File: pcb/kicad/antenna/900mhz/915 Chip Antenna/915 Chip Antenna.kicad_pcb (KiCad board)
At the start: 2 copper layers, 2 parts, among them P1 CONN_01X02, P2 CONN_01X02

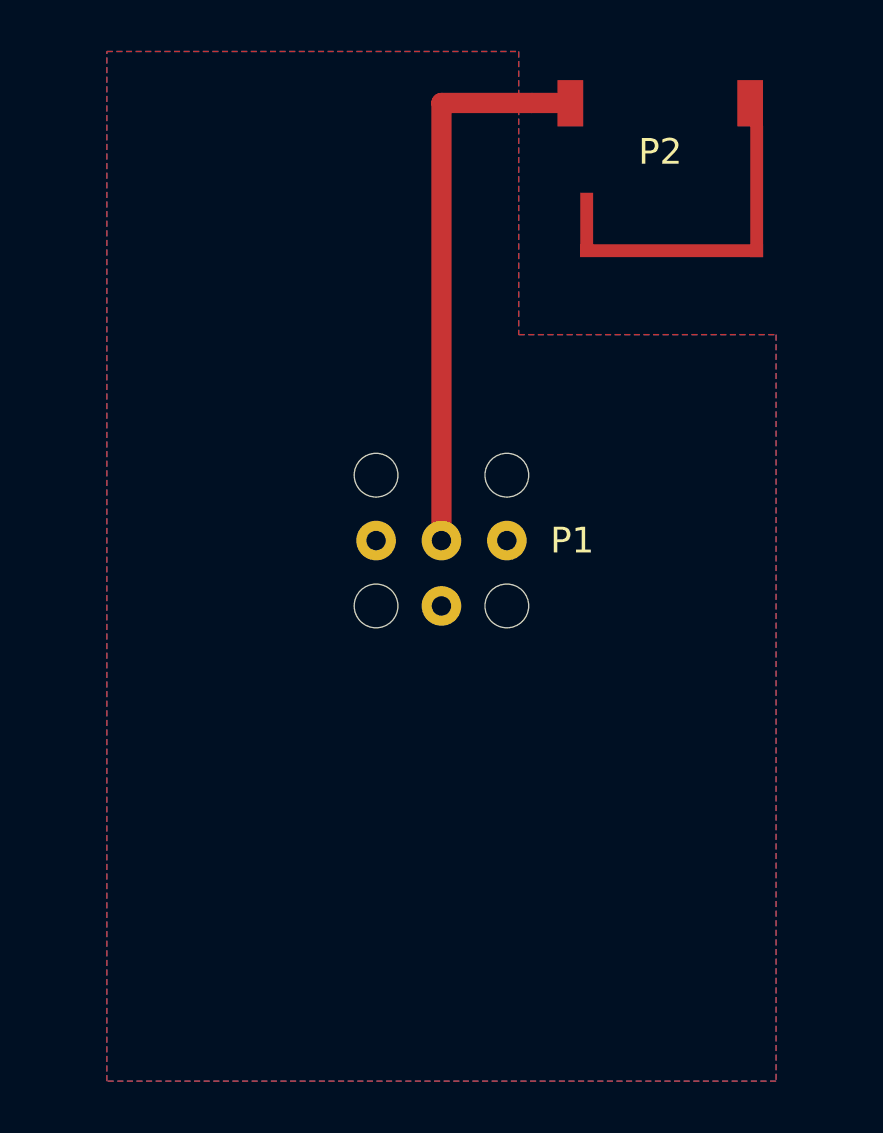
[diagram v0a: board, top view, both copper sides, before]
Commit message: Tile new antenna revisions
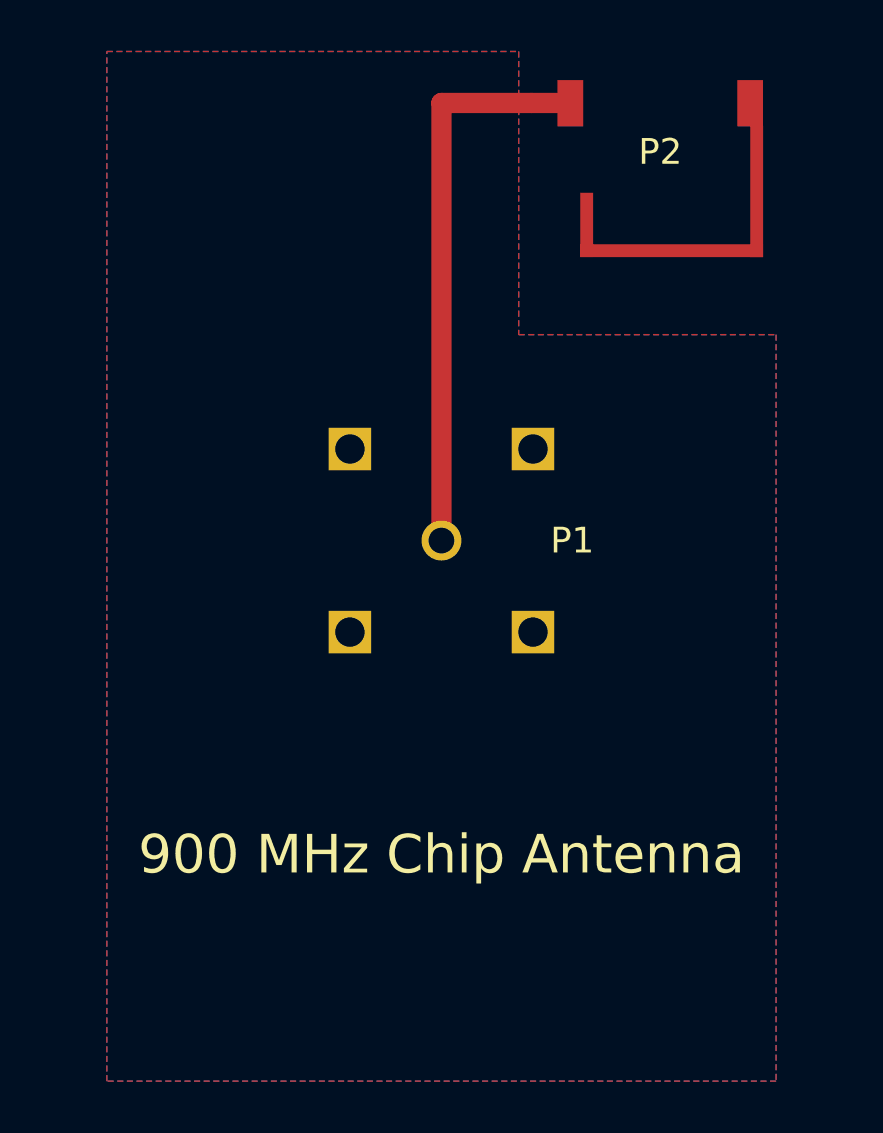
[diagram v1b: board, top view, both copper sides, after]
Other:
- board text added: "900 MHz Chip Antenna"
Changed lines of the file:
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@@
 (kicad_pcb (version 4) (host pcbnew 4.0.5)
   (general
-    (links 6)
+    (links 7)
     (no_connects 4)
-    (area 0 0 0 0)
+    (area 130.899999 74.725 157.533334 116.100001)
     (thickness 1.6)
-    (drawings 6)
+    (drawings 7)
     (tracks 3)
     (zones 0)
@@
     (mod_text_size 1 1)
     (mod_text_width 0.15)
-    (pad_size 1.54 1.54)
-    (pad_drill 0)
+    (pad_size 1.651 1.651)
+    (pad_drill 1.143)
     (pad_to_mask_clearance 0.2)
-    (aux_axis_origin 0 0)
+    (aux_axis_origin 131.0005 116.0018)
     (visible_elements 7FFFFFFF)
     (pcbplotparams
@@
       (viasonmask false)
       (mode 1)
-      (useauxorigin false)
+      (useauxorigin true)
       (hpglpennumber 1)
       (hpglpenspeed 20)
@@
       (drillshape 0)
       (scaleselection 1)
-      (outputdirectory "C:/Users/clchrist/Documents/915 Chip Antenna/GerbTool/"))
+      (outputdirectory GerbTool/))
   )
   (net 0 "")
@@
     (add_net "Net-(P1-Pad1)")
     (add_net "Net-(P2-Pad2)")
-  )
-  (module "VSMA:Vertical SMA" (layer F.Cu)
-    (at 144 95 90)
-    (fp_text reference P1 (at 0 5.08 180) (layer F.SilkS)
-      (effects (font (size 1 1) (thickness 0.15)))
-    )
-    (fp_text value CONN_01X02 (at -6 0 180) (layer F.Fab) hide
-      (effects (font (size 1 1) (thickness 0.15)))
-    )
-    (pad "" np_thru_hole circle (at -2.54 2.54 90) (size 1.7 1.7) (drill 1.7) (layers *.Cu *.Mask))
-    (pad "" np_thru_hole circle (at 2.54 -2.54 90) (size 1.7 1.7) (drill 1.7) (layers *.Cu *.Mask))
-    (pad "" np_thru_hole circle (at -2.54 -2.54 90) (size 1.7 1.7) (drill 1.7) (layers *.Cu *.Mask))
-    (pad "" np_thru_hole circle (at 2.54 2.54 90) (size 1.7 1.7) (drill 1.7) (layers *.Cu *.Mask))
-    (pad 2 thru_hole circle (at 0 -2.54 90) (size 1.54 1.54) (drill 0.754) (layers *.Cu *.Mask)
-      (net 1 GND))
-    (pad 2 thru_hole circle (at -2.54 0 90) (size 1.54 1.54) (drill 0.754) (layers *.Cu *.Mask)
-      (net 1 GND))
-    (pad 2 thru_hole circle (at 0 2.54 90) (size 1.54 1.54) (drill 0.754) (layers *.Cu *.Mask)
-      (net 1 GND))
-    (pad 1 thru_hole circle (at 0 0 90) (size 1.54 1.54) (drill 0.754) (layers *.Cu *.Mask)
-      (net 2 "Net-(P1-Pad1)"))
   )
   (module "915Chip:915 Chip Antenna" (layer F.Cu)
@@
       (net 3 "Net-(P2-Pad2)"))
   )
+  (module "VSMA:Vertical SMA" (layer F.Cu)
+    (at 144 95 90)
+    (fp_text reference P1 (at 0 5.08 180) (layer F.SilkS)
+      (effects (font (size 1 1) (thickness 0.15)))
+    )
+    (fp_text value CONN_01X02 (at -6 0 180) (layer F.Fab) hide
+      (effects (font (size 1 1) (thickness 0.15)))
+    )
+    (pad 2 thru_hole rect (at -3.556 3.556 90) (size 1.651 1.651) (drill 1.143) (layers *.Cu *.Mask)
+      (net 1 GND))
+    (pad 2 thru_hole rect (at 3.556 -3.556 90) (size 1.651 1.651) (drill 1.143) (layers *.Cu *.Mask)
+      (net 1 GND))
+    (pad 2 thru_hole rect (at -3.556 -3.556 90) (size 1.651 1.651) (drill 1.143) (layers *.Cu *.Mask)
+      (net 1 GND))
+    (pad 2 thru_hole rect (at 3.556 3.556 90) (size 1.651 1.651) (drill 1.143) (layers *.Cu *.Mask)
+      (net 1 GND))
+    (pad 1 thru_hole circle (at 0 0 90) (size 1.55 1.55) (drill 1) (layers *.Cu *.Mask)
+      (net 2 "Net-(P1-Pad1)"))
+  )
+  (gr_text "900 MHz Chip Antenna" (at 144 107.2) (layer F.SilkS)
+    (effects (font (size 1.5 1.5) (thickness 0.3)))
+  )
   (gr_line (start 157 116) (end 157 76) (angle 90) (layer Margin) (width 0.2))

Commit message: Tile uC and antenna boards
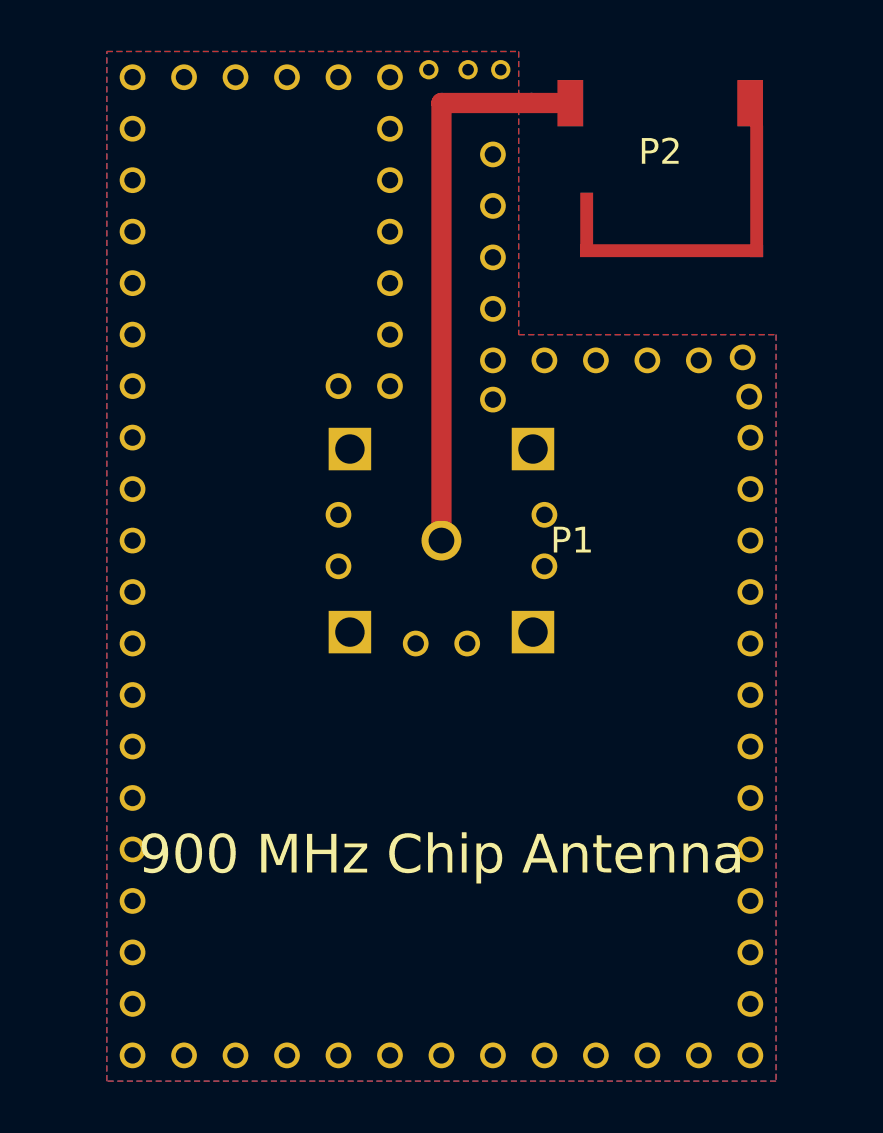
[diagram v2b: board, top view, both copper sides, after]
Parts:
- added REF**: Via_Stitch_Dia1.00mm_Drill0.64mm, Misc:Via_Stitch_Dia1.00mm_Drill0.64mm, F.Cu at (146.0, 89.5)
- added REF**: Via_Stitch_Dia1.00mm_Drill0.64mm, Misc:Via_Stitch_Dia1.00mm_Drill0.64mm, F.Cu at (146.0, 86.0)
- added REF**: Via_Stitch_Dia1.00mm_Drill0.64mm, Misc:Via_Stitch_Dia1.00mm_Drill0.64mm, F.Cu at (146.0, 88.0)
- added REF**: Via_Stitch_Dia1.00mm_Drill0.64mm, Misc:Via_Stitch_Dia1.00mm_Drill0.64mm, F.Cu at (146.0, 82.0)
- added REF**: Via_Stitch_Dia1.00mm_Drill0.64mm, Misc:Via_Stitch_Dia1.00mm_Drill0.64mm, F.Cu at (146.0, 80.0)
- added REF**: Via_Stitch_Dia1.00mm_Drill0.64mm, Misc:Via_Stitch_Dia1.00mm_Drill0.64mm, F.Cu at (145.0, 99.0)
- added REF**: Via_Stitch_Dia1.00mm_Drill0.64mm, Misc:Via_Stitch_Dia1.00mm_Drill0.64mm, F.Cu at (143.0, 99.0)
- added REF**: Via_Stitch_Dia1.00mm_Drill0.64mm, Misc:Via_Stitch_Dia1.00mm_Drill0.64mm, F.Cu at (148.0, 94.0)
- added REF**: Via_Stitch_Dia1.00mm_Drill0.64mm, Misc:Via_Stitch_Dia1.00mm_Drill0.64mm, F.Cu at (148.0, 96.0)
- added REF**: Via_Stitch_Dia1.00mm_Drill0.64mm, Misc:Via_Stitch_Dia1.00mm_Drill0.64mm, F.Cu at (140.0, 96.0)
- added REF**: Via_Stitch_Dia1.00mm_Drill0.64mm, Misc:Via_Stitch_Dia1.00mm_Drill0.64mm, F.Cu at (140.0, 94.0)
- added REF**: Via_Stitch_Dia0.508mm_Drill0.254mm, Misc:Via_Stitch_Dia0.508mm_Drill0.254mm, F.Cu at (146.3, 76.7)
- added REF**: Via_Stitch_Dia1.00mm_Drill0.64mm, Misc:Via_Stitch_Dia1.00mm_Drill0.64mm, F.Cu at (140.0, 89.0)
- added REF**: Via_Stitch_Dia1.00mm_Drill0.64mm, Misc:Via_Stitch_Dia1.00mm_Drill0.64mm, F.Cu at (142.0, 79.0)
- added REF**: Via_Stitch_Dia1.00mm_Drill0.64mm, Misc:Via_Stitch_Dia1.00mm_Drill0.64mm, F.Cu at (142.0, 81.0)
- added REF**: Via_Stitch_Dia1.00mm_Drill0.64mm, Misc:Via_Stitch_Dia1.00mm_Drill0.64mm, F.Cu at (142.0, 83.0)
- added REF**: Via_Stitch_Dia1.00mm_Drill0.64mm, Misc:Via_Stitch_Dia1.00mm_Drill0.64mm, F.Cu at (142.0, 89.0)
- added REF**: Via_Stitch_Dia1.00mm_Drill0.64mm, Misc:Via_Stitch_Dia1.00mm_Drill0.64mm, F.Cu at (142.0, 87.0)
- added REF**: Via_Stitch_Dia1.00mm_Drill0.64mm, Misc:Via_Stitch_Dia1.00mm_Drill0.64mm, F.Cu at (142.0, 85.0)
- added REF**: Via_Stitch_Dia1.00mm_Drill0.64mm, Misc:Via_Stitch_Dia1.00mm_Drill0.64mm, F.Cu at (142.0, 77.0)
- added REF**: Via_Stitch_Dia1.00mm_Drill0.64mm, Misc:Via_Stitch_Dia1.00mm_Drill0.64mm, F.Cu at (138.0, 77.0)
- added REF**: Via_Stitch_Dia1.00mm_Drill0.64mm, Misc:Via_Stitch_Dia1.00mm_Drill0.64mm, F.Cu at (140.0, 77.0)
- added REF**: Via_Stitch_Dia0.508mm_Drill0.254mm, Misc:Via_Stitch_Dia0.508mm_Drill0.254mm, F.Cu at (145.0, 76.7)
- added REF**: Via_Stitch_Dia1.00mm_Drill0.64mm, Misc:Via_Stitch_Dia1.00mm_Drill0.64mm, F.Cu at (136.0, 77.0)
- added REF**: Via_Stitch_Dia1.00mm_Drill0.64mm, Misc:Via_Stitch_Dia1.00mm_Drill0.64mm, F.Cu at (134.0, 77.0)
- added REF**: Via_Stitch_Dia1.00mm_Drill0.64mm, Misc:Via_Stitch_Dia1.00mm_Drill0.64mm, F.Cu at (156.0, 91.0)
- added REF**: Via_Stitch_Dia1.00mm_Drill0.64mm, Misc:Via_Stitch_Dia1.00mm_Drill0.64mm, F.Cu at (156.0, 89.4)
- added REF**: Via_Stitch_Dia1.00mm_Drill0.64mm, Misc:Via_Stitch_Dia1.00mm_Drill0.64mm, F.Cu at (156.0, 101.0)
- added REF**: Via_Stitch_Dia1.00mm_Drill0.64mm, Misc:Via_Stitch_Dia1.00mm_Drill0.64mm, F.Cu at (156.0, 103.0)
- added REF**: Via_Stitch_Dia1.00mm_Drill0.64mm, Misc:Via_Stitch_Dia1.00mm_Drill0.64mm, F.Cu at (156.0, 105.0)
- added REF**: Via_Stitch_Dia1.00mm_Drill0.64mm, Misc:Via_Stitch_Dia1.00mm_Drill0.64mm, F.Cu at (156.0, 107.0)
- added REF**: Via_Stitch_Dia1.00mm_Drill0.64mm, Misc:Via_Stitch_Dia1.00mm_Drill0.64mm, F.Cu at (156.0, 99.0)
- added REF**: Via_Stitch_Dia1.00mm_Drill0.64mm, Misc:Via_Stitch_Dia1.00mm_Drill0.64mm, F.Cu at (156.0, 97.0)
- added REF**: Via_Stitch_Dia1.00mm_Drill0.64mm, Misc:Via_Stitch_Dia1.00mm_Drill0.64mm, F.Cu at (155.7, 87.9)
- added REF**: Via_Stitch_Dia1.00mm_Drill0.64mm, Misc:Via_Stitch_Dia1.00mm_Drill0.64mm, F.Cu at (156.0, 95.0)
- added REF**: Via_Stitch_Dia1.00mm_Drill0.64mm, Misc:Via_Stitch_Dia1.00mm_Drill0.64mm, F.Cu at (156.0, 93.0)
- added REF**: Via_Stitch_Dia1.00mm_Drill0.64mm, Misc:Via_Stitch_Dia1.00mm_Drill0.64mm, F.Cu at (156.0, 113.0)
- added REF**: Via_Stitch_Dia1.00mm_Drill0.64mm, Misc:Via_Stitch_Dia1.00mm_Drill0.64mm, F.Cu at (156.0, 111.0)
- added REF**: Via_Stitch_Dia1.00mm_Drill0.64mm, Misc:Via_Stitch_Dia1.00mm_Drill0.64mm, F.Cu at (156.0, 109.0)
- added REF**: Via_Stitch_Dia1.00mm_Drill0.64mm, Misc:Via_Stitch_Dia1.00mm_Drill0.64mm, F.Cu at (156.0, 115.0)
- added REF**: Via_Stitch_Dia1.00mm_Drill0.64mm, Misc:Via_Stitch_Dia1.00mm_Drill0.64mm, F.Cu at (152.0, 115.0)
- added REF**: Via_Stitch_Dia1.00mm_Drill0.64mm, Misc:Via_Stitch_Dia1.00mm_Drill0.64mm, F.Cu at (154.0, 115.0)
- added REF**: Via_Stitch_Dia1.00mm_Drill0.64mm, Misc:Via_Stitch_Dia1.00mm_Drill0.64mm, F.Cu at (150.0, 115.0)
- added REF**: Via_Stitch_Dia1.00mm_Drill0.64mm, Misc:Via_Stitch_Dia1.00mm_Drill0.64mm, F.Cu at (148.0, 115.0)
- added REF**: Via_Stitch_Dia1.00mm_Drill0.64mm, Misc:Via_Stitch_Dia1.00mm_Drill0.64mm, F.Cu at (154.0, 88.0)
- added REF**: Via_Stitch_Dia1.00mm_Drill0.64mm, Misc:Via_Stitch_Dia1.00mm_Drill0.64mm, F.Cu at (140.0, 115.0)
- added REF**: Via_Stitch_Dia1.00mm_Drill0.64mm, Misc:Via_Stitch_Dia1.00mm_Drill0.64mm, F.Cu at (142.0, 115.0)
- added REF**: Via_Stitch_Dia1.00mm_Drill0.64mm, Misc:Via_Stitch_Dia1.00mm_Drill0.64mm, F.Cu at (146.0, 115.0)
- added REF**: Via_Stitch_Dia1.00mm_Drill0.64mm, Misc:Via_Stitch_Dia1.00mm_Drill0.64mm, F.Cu at (144.0, 115.0)
- added REF**: Via_Stitch_Dia1.00mm_Drill0.64mm, Misc:Via_Stitch_Dia1.00mm_Drill0.64mm, F.Cu at (136.0, 115.0)
- added REF**: Via_Stitch_Dia1.00mm_Drill0.64mm, Misc:Via_Stitch_Dia1.00mm_Drill0.64mm, F.Cu at (138.0, 115.0)
- added REF**: Via_Stitch_Dia1.00mm_Drill0.64mm, Misc:Via_Stitch_Dia1.00mm_Drill0.64mm, F.Cu at (134.0, 115.0)
- added REF**: Via_Stitch_Dia1.00mm_Drill0.64mm, Misc:Via_Stitch_Dia1.00mm_Drill0.64mm, F.Cu at (132.0, 109.0)
- added REF**: Via_Stitch_Dia1.00mm_Drill0.64mm, Misc:Via_Stitch_Dia1.00mm_Drill0.64mm, F.Cu at (132.0, 111.0)
- added REF**: Via_Stitch_Dia1.00mm_Drill0.64mm, Misc:Via_Stitch_Dia1.00mm_Drill0.64mm, F.Cu at (132.0, 113.0)
- added REF**: Via_Stitch_Dia1.00mm_Drill0.64mm, Misc:Via_Stitch_Dia1.00mm_Drill0.64mm, F.Cu at (148.0, 88.0)
- added REF**: Via_Stitch_Dia1.00mm_Drill0.64mm, Misc:Via_Stitch_Dia1.00mm_Drill0.64mm, F.Cu at (132.0, 115.0)
- added REF**: Via_Stitch_Dia1.00mm_Drill0.64mm, Misc:Via_Stitch_Dia1.00mm_Drill0.64mm, F.Cu at (132.0, 93.0)
- added REF**: Via_Stitch_Dia1.00mm_Drill0.64mm, Misc:Via_Stitch_Dia1.00mm_Drill0.64mm, F.Cu at (132.0, 95.0)
- added REF**: Via_Stitch_Dia1.00mm_Drill0.64mm, Misc:Via_Stitch_Dia1.00mm_Drill0.64mm, F.Cu at (132.0, 97.0)
- added REF**: Via_Stitch_Dia1.00mm_Drill0.64mm, Misc:Via_Stitch_Dia1.00mm_Drill0.64mm, F.Cu at (132.0, 99.0)
- added REF**: Via_Stitch_Dia1.00mm_Drill0.64mm, Misc:Via_Stitch_Dia1.00mm_Drill0.64mm, F.Cu at (132.0, 107.0)
- added REF**: Via_Stitch_Dia1.00mm_Drill0.64mm, Misc:Via_Stitch_Dia1.00mm_Drill0.64mm, F.Cu at (132.0, 105.0)
- added REF**: Via_Stitch_Dia1.00mm_Drill0.64mm, Misc:Via_Stitch_Dia1.00mm_Drill0.64mm, F.Cu at (132.0, 103.0)
- added REF**: Via_Stitch_Dia1.00mm_Drill0.64mm, Misc:Via_Stitch_Dia1.00mm_Drill0.64mm, F.Cu at (132.0, 101.0)
- added REF**: Via_Stitch_Dia1.00mm_Drill0.64mm, Misc:Via_Stitch_Dia1.00mm_Drill0.64mm, F.Cu at (132.0, 85.0)
- added REF**: Via_Stitch_Dia1.00mm_Drill0.64mm, Misc:Via_Stitch_Dia1.00mm_Drill0.64mm, F.Cu at (152.0, 88.0)
- added REF**: Via_Stitch_Dia1.00mm_Drill0.64mm, Misc:Via_Stitch_Dia1.00mm_Drill0.64mm, F.Cu at (132.0, 87.0)
- added REF**: Via_Stitch_Dia1.00mm_Drill0.64mm, Misc:Via_Stitch_Dia1.00mm_Drill0.64mm, F.Cu at (132.0, 89.0)
- added REF**: Via_Stitch_Dia1.00mm_Drill0.64mm, Misc:Via_Stitch_Dia1.00mm_Drill0.64mm, F.Cu at (132.0, 91.0)
- added REF**: Via_Stitch_Dia1.00mm_Drill0.64mm, Misc:Via_Stitch_Dia1.00mm_Drill0.64mm, F.Cu at (132.0, 83.0)
- added REF**: Via_Stitch_Dia1.00mm_Drill0.64mm, Misc:Via_Stitch_Dia1.00mm_Drill0.64mm, F.Cu at (132.0, 81.0)
- added REF**: Via_Stitch_Dia1.00mm_Drill0.64mm, Misc:Via_Stitch_Dia1.00mm_Drill0.64mm, F.Cu at (132.0, 79.0)
- added REF**: Via_Stitch_Dia1.00mm_Drill0.64mm, Misc:Via_Stitch_Dia1.00mm_Drill0.64mm, F.Cu at (132.0, 77.0)
- added REF**: Via_Stitch_Dia0.508mm_Drill0.254mm, Misc:Via_Stitch_Dia0.508mm_Drill0.254mm, F.Cu at (143.5, 76.7)
- added REF**: Via_Stitch_Dia1.00mm_Drill0.64mm, Misc:Via_Stitch_Dia1.00mm_Drill0.64mm, F.Cu at (150.0, 88.0)
- added REF**: Via_Stitch_Dia1.00mm_Drill0.64mm, Misc:Via_Stitch_Dia1.00mm_Drill0.64mm, F.Cu at (146.0, 84.0)
